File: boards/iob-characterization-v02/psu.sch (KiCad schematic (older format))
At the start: 20 parts, among them U1 ISL24021IRT065Z-T7A‎, U11 SIP32409, U12 SIP32409, U18 LDO1117-25, U19 TCA6424A, U20 INA226

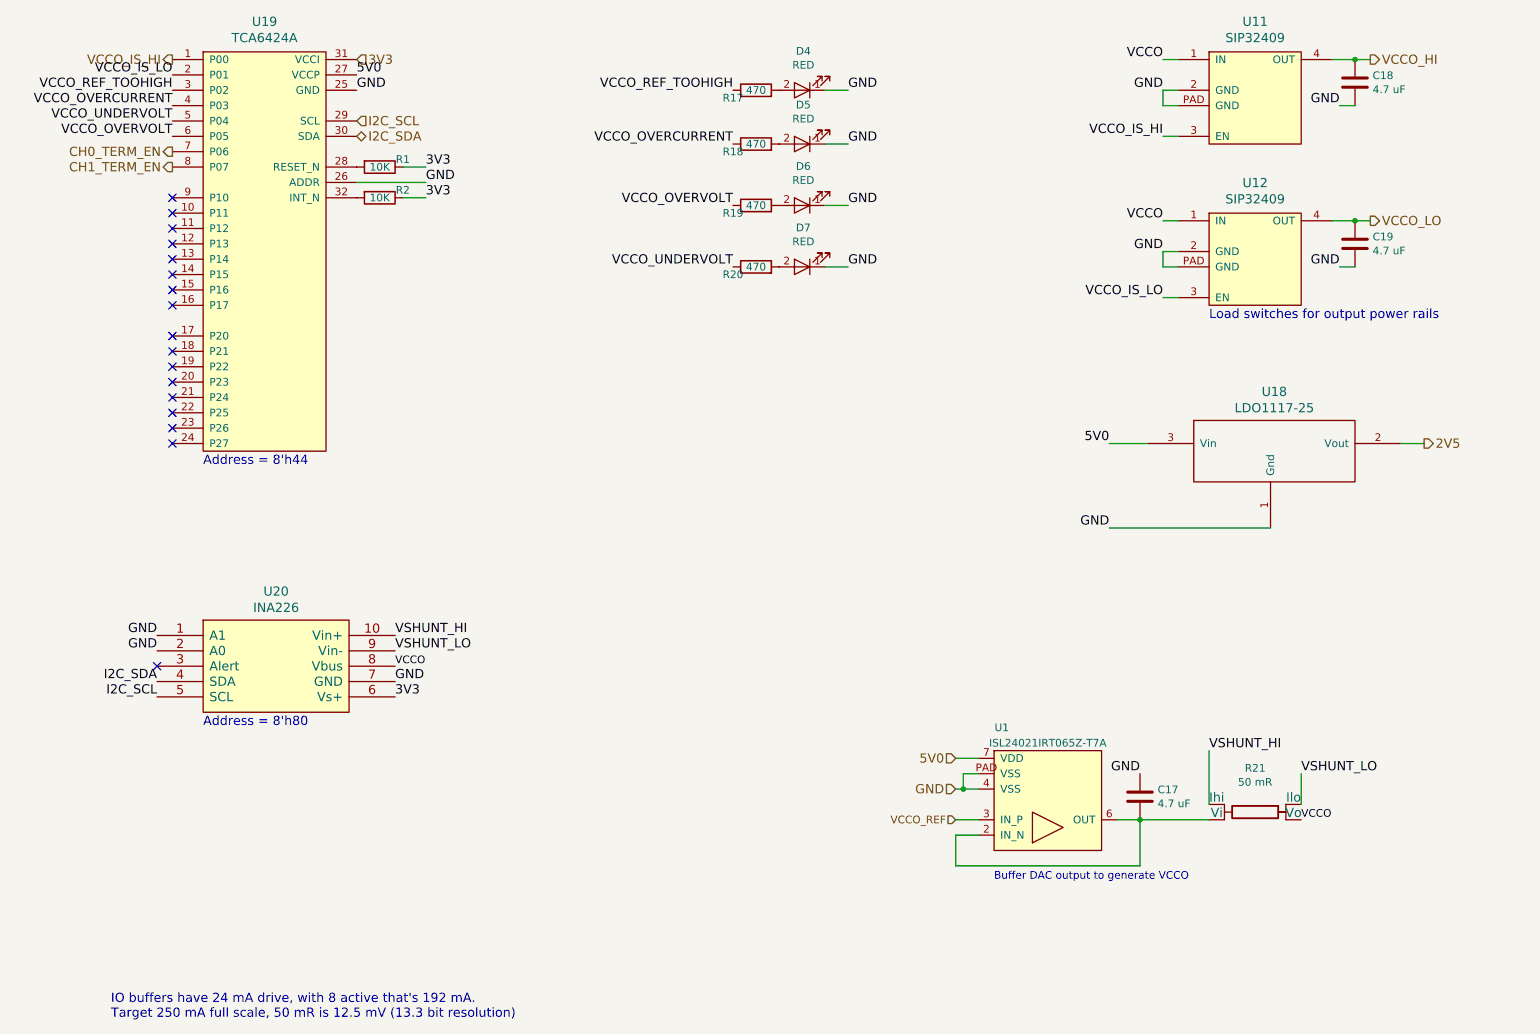
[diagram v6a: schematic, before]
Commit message: Finished initial layout. Still needs planes plus full design review.
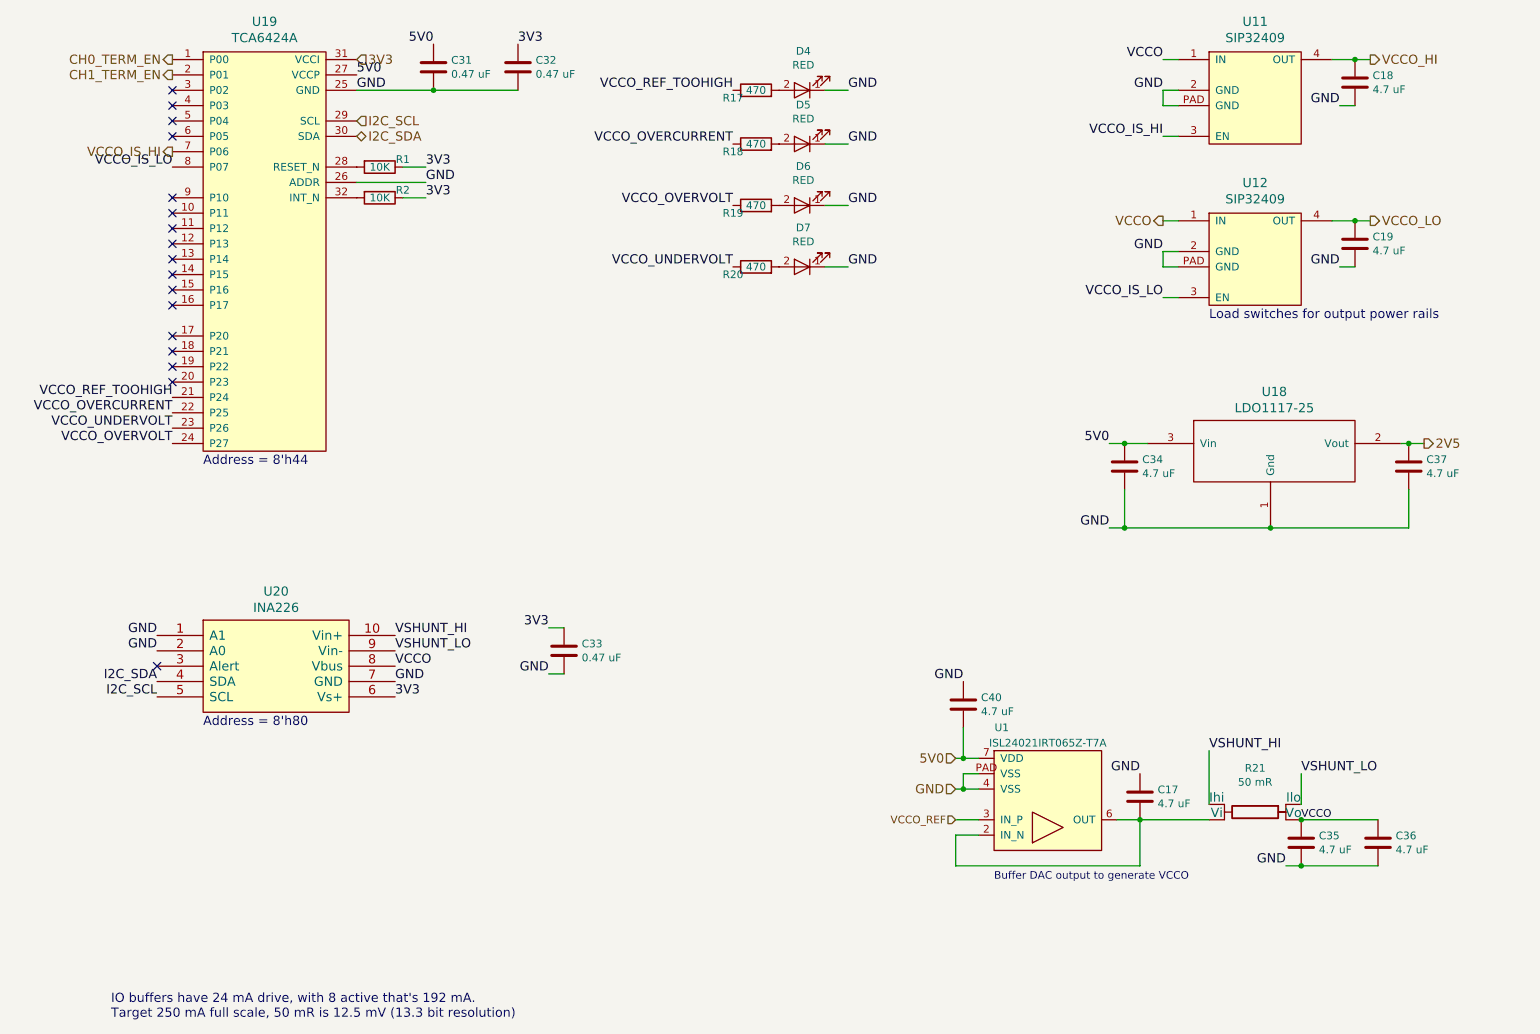
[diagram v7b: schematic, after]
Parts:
- added C31, C32, C33: 0.47 uF, azonenberg_pcb:EIA_0402_CAP_NOSILK, symbol device:C
- added C34, C35, C36, C37, C40: 4.7 uF, azonenberg_pcb:EIA_0603_CAP_NOSILK, symbol device:C
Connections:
- net 2V5: now also C37.1
- net 3V3: now also C32.1, C33.1
- net 5V0: now also C31.1, C34.1, C40.2
- net CH0_TERM_EN: now also U19.1 (P00); no longer U19.7 (P06)
- net CH1_TERM_EN: now also U19.2 (P01); no longer U19.8 (P07)
- net GND: now also C31.2, C32.2, C33.2, C34.2, C35.2, C36.2, C37.2, C40.1
- net VCCO: now also C35.1, C36.1
- net VCCO_IS_HI: now also U19.7 (P06); no longer U19.1 (P00)
- net VCCO_IS_LO: now also U19.8 (P07); no longer U19.2 (P01)
- net VCCO_OVERCURRENT: now also U19.22 (P25); no longer U19.4 (P03)
- net VCCO_OVERVOLT: now also U19.24 (P27); no longer U19.6 (P05)
- net VCCO_REF_TOOHIGH: now also U19.21 (P24); no longer U19.3 (P02)
- net VCCO_UNDERVOLT: now also U19.23 (P26); no longer U19.5 (P04)
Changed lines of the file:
@@
 Wire Wire Line
 	9900 1900 9800 1900
-Text Label 8550 1900 2    60   ~ 0
-VCCO
 Text Label 8550 1050 2    60   ~ 0
 GND
@@
 	7200 5600 7250 5600
 Wire Wire Line
-	7350 5400 7200 5400
+	7350 5400 7250 5400
 Text Label 9450 5800 0    50   ~ 0
 VCCO
@@
 Text Notes 7450 6200 0    50   ~ 0
 Buffer DAC output to generate VCCO
-Text HLabel 2100 850  0    60   Output ~ 0
+Text HLabel 2100 1450 0    60   Output ~ 0
 VCCO_IS_HI
 Text Label 8550 1350 2    60   ~ 0
@@
 Text Label 8550 2400 2    60   ~ 0
 VCCO_IS_LO
-Text Label 2100 950  2    60   ~ 0
+Text Label 2100 1550 2    60   ~ 0
 VCCO_IS_LO
 $Comp
@@
 $EndComp
 Wire Wire Line
-	10250 3350 10100 3350
+	10250 3350 10150 3350
 Text Label 8200 3900 2    60   ~ 0
 GND
 Wire Wire Line
-	8200 3900 9250 3900
+	8200 3900 8300 3900
 Text Label 8200 3350 2    60   ~ 0
 5V0
 Wire Wire Line
-	8200 3350 8450 3350
+	8200 3350 8300 3350
 $Comp
 L device:C C19
@@
 Text Notes 2300 3500 0    60   ~ 0
 Address = 8'h44
-Text Label 2100 1050 2    60   ~ 0
+Text Label 2100 3050 2    60   ~ 0
 VCCO_REF_TOOHIGH
 Text Label 5750 1050 2    60   ~ 0
@@
 Wire Wire Line
 	6500 1050 6350 1050
-NoConn ~ 2100 3350
-NoConn ~ 2100 3250
-NoConn ~ 2100 3150
-NoConn ~ 2100 3050
 NoConn ~ 2100 2950
 NoConn ~ 2100 2850
@@
 $EndComp
 NoConn ~ 2000 4800
-Text Label 2100 1150 2    60   ~ 0
-VCCO_OVERCURRENT
-Text Label 2100 1250 2    60   ~ 0
-VCCO_UNDERVOLT
-Text Label 2100 1350 2    60   ~ 0
+Text Label 2100 3350 2    60   ~ 0
 VCCO_OVERVOLT
 Text Label 5750 1400 2    60   ~ 0
@@
 Text Label 3550 4600 0    60   ~ 0
 VSHUNT_HI
-Text Label 3550 4800 0    50   ~ 0
+Text Label 3550 4800 0    60   ~ 0
 VCCO
 Text Label 3550 5000 0    60   ~ 0
@@
 Wire Wire Line
 	7250 5600 7350 5600
-Text HLabel 2100 1450 0    60   Output ~ 0
+Text HLabel 2100 850  0    60   Output ~ 0
 CH0_TERM_EN
-Text HLabel 2100 1550 0    60   Output ~ 0
+Text HLabel 2100 950  0    60   Output ~ 0
 CH1_TERM_EN
+$Comp
+L device:C C33
+U 1 1 5B756701
+P 4650 4700
+F 0 "C33" H 4765 4746 50  0000 L CNN
+F 1 "0.47 uF" H 4765 4655 50  0000 L CNN
+F 2 "azonenberg_pcb:EIA_0402_CAP_NOSILK" H 4688 4550 50  0001 C CNN
+F 3 "" H 4650 4700 50  0001 C CNN
+	1    4650 4700
+	1    0    0    -1
+$EndComp
+Text Label 4550 4850 2    60   ~ 0
+GND
+Wire Wire Line
+	4550 4850 4650 4850
+Text Label 4550 4550 2    60   ~ 0
+3V3
+Wire Wire Line
+	4550 4550 4650 4550
+$Comp
+L device:C C31
+U 1 1 5B7581DB
+P 3800 900
+F 0 "C31" H 3915 946 50  0000 L CNN
+F 1 "0.47 uF" H 3915 855 50  0000 L CNN
+F 2 "azonenberg_pcb:EIA_0402_CAP_NOSILK" H 3838 750 50  0001 C CNN
+F 3 "" H 3800 900 50  0001 C CNN
+	1    3800 900
+	1    0    0    -1
+$EndComp
+Text Label 3800 750  2    60   ~ 0
+5V0
+$Comp
+L device:C C32
+U 1 1 5B7582FB
+P 4350 900
+F 0 "C32" H 4465 946 50  0000 L CNN
+F 1 "0.47 uF" H 4465 855 50  0000 L CNN
+F 2 "azonenberg_pcb:EIA_0402_CAP_NOSILK" H 4388 750 50  0001 C CNN
+F 3 "" H 4350 900 50  0001 C CNN
+	1    4350 900
+	1    0    0    -1
+$EndComp
+Text Label 4350 750  0    60   ~ 0
+3V3
+Wire Wire Line
+	3300 1050 3800 1050
+Wire Wire Line
+	3800 1050 4350 1050
+Connection ~ 3800 1050
+$Comp
+L device:C C35
+U 1 1 5B75BD34
+P 9450 5950
+F 0 "C35" H 9565 5996 50  0000 L CNN
+F 1 "4.7 uF" H 9565 5905 50  0000 L CNN
+F 2 "azonenberg_pcb:EIA_0603_CAP_NOSILK" H 9488 5800 50  0001 C CNN
+F 3 "" H 9450 5950 50  0001 C CNN
+	1    9450 5950
+	1    0    0    -1
+$EndComp
+$Comp
+L device:C C36
+U 1 1 5B75BDE0
+P 9950 5950
+F 0 "C36" H 10065 5996 50  0000 L CNN
+F 1 "4.7 uF" H 10065 5905 50  0000 L CNN
+F 2 "azonenberg_pcb:EIA_0603_CAP_NOSILK" H 9988 5800 50  0001 C CNN
+F 3 "" H 9950 5950 50  0001 C CNN
+	1    9950 5950
+	1    0    0    -1
+$EndComp
+Wire Wire Line
+	9950 5800 9450 5800
+Connection ~ 9450 5800
+Wire Wire Line
+	9450 6100 9950 6100
+Text Label 9350 6100 2    60   ~ 0
+GND
+Wire Wire Line
+	9350 6100 9450 6100
+Connection ~ 9450 6100
+$Comp
+L device:C C34
+U 1 1 5B75F0B2
+P 8300 3500
+F 0 "C34" H 8415 3546 50  0000 L CNN
+F 1 "4.7 uF" H 8415 3455 50  0000 L CNN
+F 2 "azonenberg_pcb:EIA_0603_CAP_NOSILK" H 8338 3350 50  0001 C CNN
+F 3 "" H 8300 3500 50  0001 C CNN
+	1    8300 3500
+	1    0    0    -1
+$EndComp
+Connection ~ 8300 3350
+Wire Wire Line
+	8300 3350 8450 3350
+$Comp
+L device:C C37
+U 1 1 5B75F19A
+P 10150 3500
+F 0 "C37" H 10265 3546 50  0000 L CNN
+F 1 "4.7 uF" H 10265 3455 50  0000 L CNN
+F 2 "azonenberg_pcb:EIA_0603_CAP_NOSILK" H 10188 3350 50  0001 C CNN
+F 3 "" H 10150 3500 50  0001 C CNN
+	1    10150 3500
+	1    0    0    -1
+$EndComp
+Connection ~ 10150 3350
+Wire Wire Line
+	10150 3350 10100 3350
+Wire Wire Line
+	10150 3650 10150 3900
+Wire Wire Line
+	10150 3900 9250 3900
+Connection ~ 9250 3900
+Wire Wire Line
+	8300 3650 8300 3900
+Connection ~ 8300 3900
+Wire Wire Line
+	8300 3900 9250 3900
+$Comp
+L device:C C40
+U 1 1 5B76B3AA
+P 7250 5050
+F 0 "C40" H 7365 5096 50  0000 L CNN
+F 1 "4.7 uF" H 7365 5005 50  0000 L CNN
+F 2 "azonenberg_pcb:EIA_0603_CAP_NOSILK" H 7288 4900 50  0001 C CNN
+F 3 "" H 7250 5050 50  0001 C CNN
+	1    7250 5050
+	1    0    0    -1
+$EndComp
+Wire Wire Line
+	7250 5200 7250 5400
+Connection ~ 7250 5400
+Wire Wire Line
+	7250 5400 7200 5400
+Text Label 7250 4900 2    60   ~ 0
+GND
+Text Label 2100 3150 2    60   ~ 0
+VCCO_OVERCURRENT
+Text Label 2100 3250 2    60   ~ 0
+VCCO_UNDERVOLT
+NoConn ~ 2100 1350
+NoConn ~ 2100 1250
+NoConn ~ 2100 1150
+NoConn ~ 2100 1050
+Text HLabel 8550 1900 0    60   Output ~ 0
+VCCO
 $EndSCHEMATC
